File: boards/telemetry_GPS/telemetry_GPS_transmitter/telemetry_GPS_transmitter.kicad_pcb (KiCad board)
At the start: 2 copper layers, 64 parts, among them J1 Conn_02x05_Odd_Even, J2 Conn_01x03, J3 Conn_01x03, J4 Conn_Coaxial, J5 54602-908LF, SW1 SW_Push, U1 STM32WL55CCUx, U2 TLV75509PDBV, U3 STLINK-V3MODS, U4 BALFHB-WL-02D3, U5 MASW-007221, U6 74AHC1G04SE-7, U7 NEO-M8N, U8 ISO1042QDWVQ1, U9 MCP2515-xST

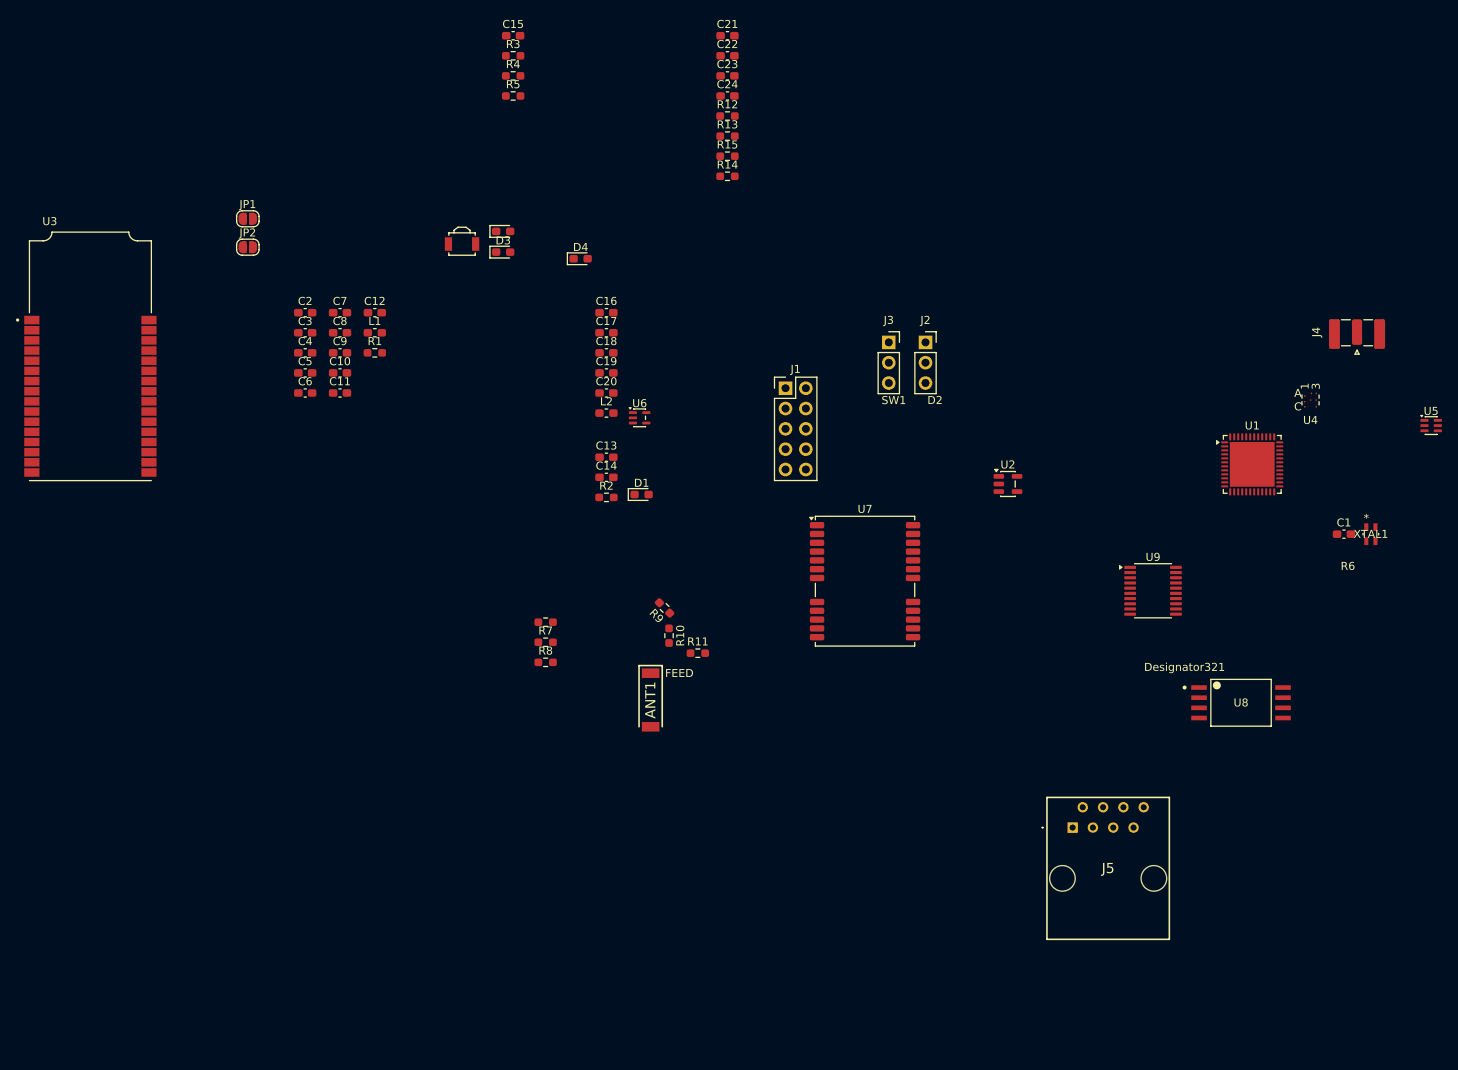
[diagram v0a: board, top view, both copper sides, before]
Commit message: Routed GPS antenna-to-transceiver and SMA port to MCU, still need copper pours, connections to CAN, and all other pins
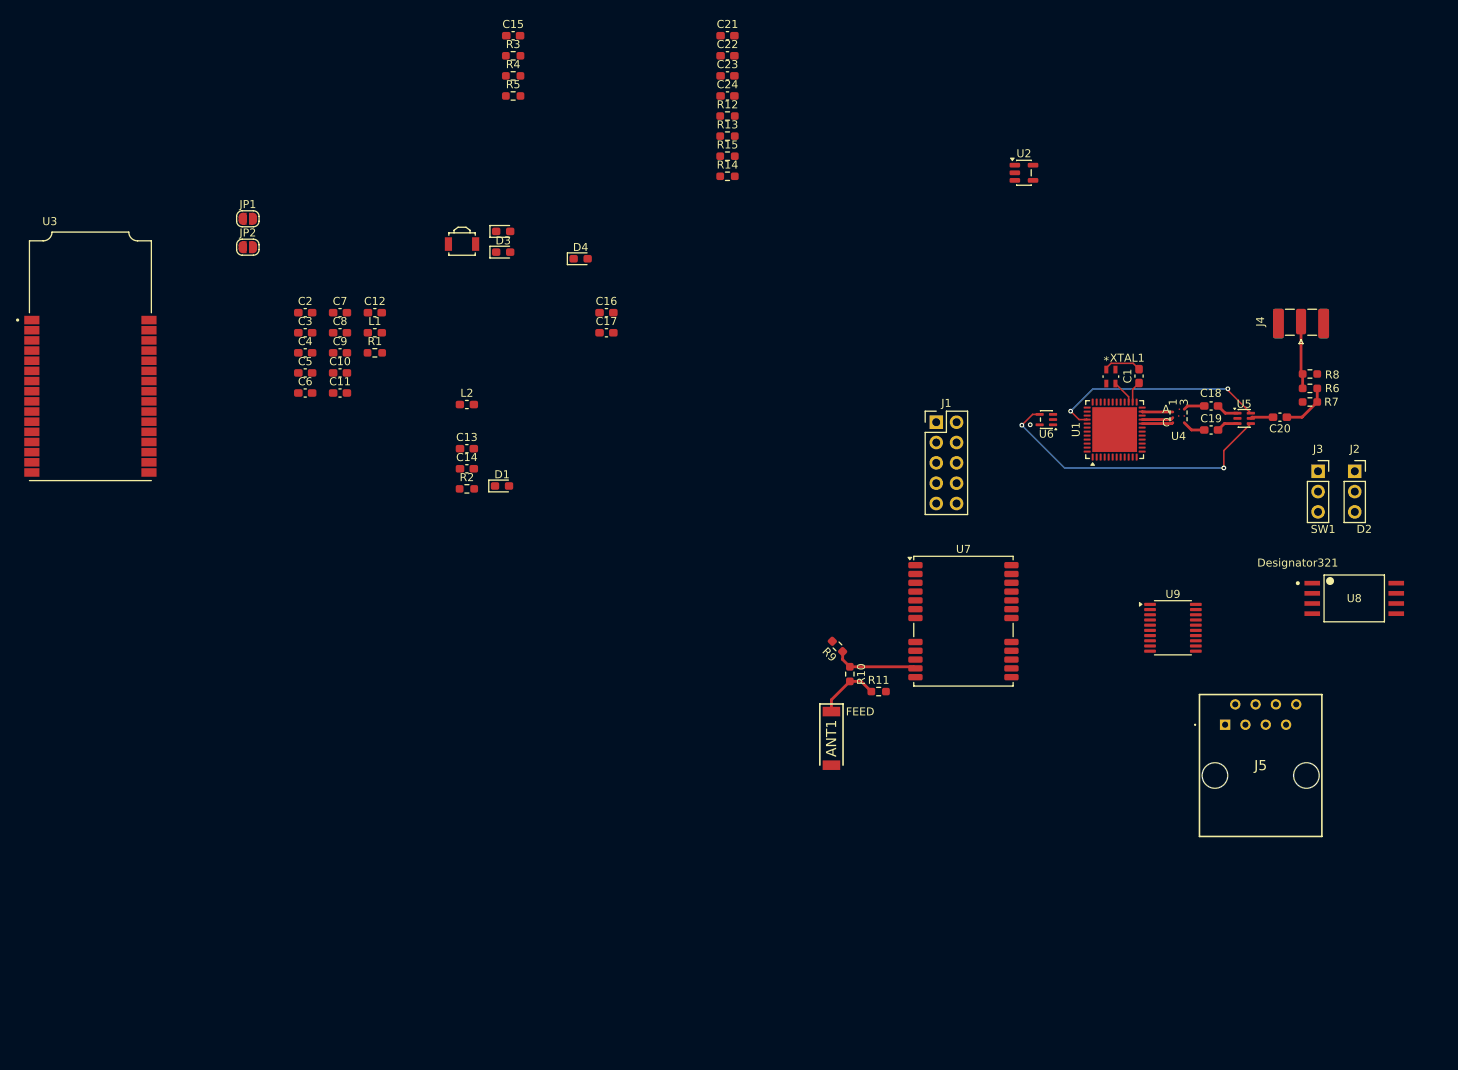
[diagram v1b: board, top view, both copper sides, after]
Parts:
- moved R8 102.1 mm to (184.6, 69.9)
- moved R7 100.7 mm to (184.6, 71.7), turned to 180 degrees
- moved R6 99.4 mm to (184.6, 73.4), turned to 180 degrees
- moved C20 84.2 mm to (180.9, 75.3), turned to 180 degrees
- moved C19 75.9 mm to (172.3, 76.9)
- moved C18 75.9 mm to (172.3, 73.9), turned to 180 degrees
- moved J2 56.0 mm to (190.2, 82.1)
- moved J3 56.0 mm to (185.6, 82.1)
- moved U6 50.8 mm to (151.7, 75.6), turned to 180 degrees
- moved U2 39.0 mm to (148.9, 44.8)
- moved XTAL1 38.0 mm to (159.7, 70.2)
- moved C1 32.4 mm to (163.2, 70.2), turned to 90 degrees
- moved U5 23.4 mm to (176.4, 75.5)
- moved ANT1 23.1 mm to (124.8, 115.5)
- moved R10 23.1 mm to (127.1, 107.4)
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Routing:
- net Net-(U5-V2): track 0.00 -> 37.2 mm, vias 0 -> 2
- net /RF/RF_TX_EN: track 0.00 -> 27.7 mm, vias 0 -> 2
- net Net-(U7-RF_IN): track 0.00 -> 10.6 mm
- net Net-(J4-In): track 0.00 -> 8.43 mm
- net Net-(ANT1-FEED): track 0.00 -> 7.94 mm
- net Net-(C20-Pad1): track 0.00 -> 6.29 mm
- net Net-(C1-Pad2): track 0.00 -> 4.84 mm
- net /RF/RFI_N: track 0.00 -> 3.93 mm
- net /RF/RFI_P: track 0.00 -> 3.88 mm
- net /RF/RFO_HP: track 0.00 -> 3.85 mm
- net Net-(U5-RFC): track 0.00 -> 3.25 mm
- net /STM32/OSC_OUT: track 0.00 -> 3.00 mm
- net /RF/RF_I: track 0.00 -> 2.88 mm
- net Net-(U5-RF1): track 0.00 -> 2.80 mm
- net Net-(U5-RF2): track 0.00 -> 2.76 mm
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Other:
- copper layers 2 -> 4

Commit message: Pushing some antenna routing stuff
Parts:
- added H1: MountingHole, MountingHole:MountingHole_4.3mm_M4, F.Cu at (82.6, 122.3)
- added H2: MountingHole, MountingHole:MountingHole_4.3mm_M4, F.Cu at (82.6, 132.4)
- added H3: MountingHole, MountingHole:MountingHole_4.3mm_M4, F.Cu at (82.6, 142.6)
- added H4: MountingHole, MountingHole:MountingHole_4.3mm_M4, F.Cu at (82.6, 152.7)
- moved R1 105.3 mm to (172.1, 81.3)
- moved SW1 104.3 mm to (177.6, 86.6)
- moved U2 24.8 mm to (142.2, 68.6)
- moved J1 9.18 mm to (128.8, 74.9)
- moved U7 7.76 mm to (134.5, 104.5)
- moved ANT1 7.76 mm to (118.0, 119.2)
- moved R9 7.76 mm to (118.7, 107.7)
- moved R10 7.76 mm to (120.3, 111.1)
- moved R11 7.76 mm to (123.9, 113.3)
- moved J5 7.69 mm to (174.2, 106.0)
- moved U9 6.14 mm to (169.2, 95.7), turned to 180 degrees
- moved U8 3.09 mm to (187.8, 95.9)
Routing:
- net Net-(U1-PH3): track 0.00 -> 9.51 mm
- net Net-(U5-V2): track 37.2 -> 36.0 mm, vias 2 -> 3
